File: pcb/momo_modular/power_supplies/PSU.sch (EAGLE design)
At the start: 24 parts, among them IC1 MAX1555

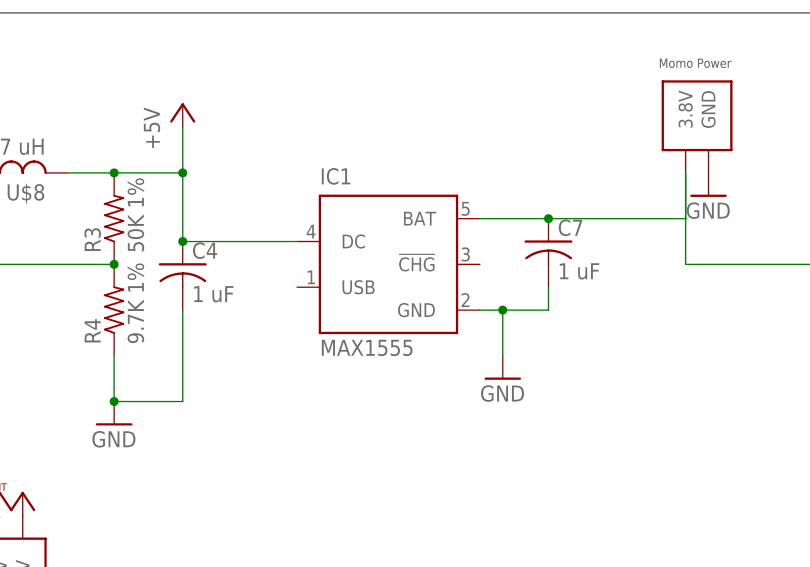
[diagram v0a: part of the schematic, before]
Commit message: Updated schematic and layout to reflect capacitor changes
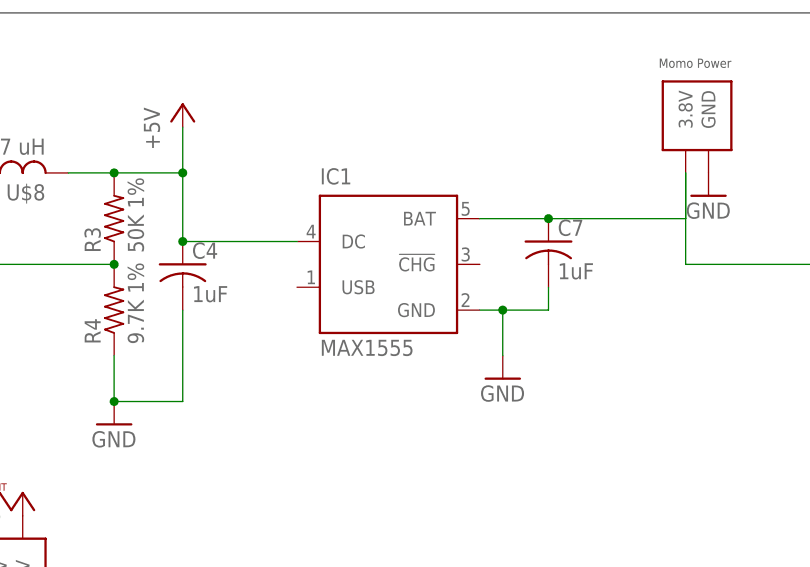
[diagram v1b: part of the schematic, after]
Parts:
- C4, C7: value 1 uF -> 1uF; device rcl:C-USC0805 -> rcl:C-USC0402
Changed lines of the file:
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@@
 <part name="IC1" library="maxim" deviceset="MAX1555" device=""/>
 <part name="GND6" library="supply1" deviceset="GND" device=""/>
-<part name="C4" library="rcl" deviceset="C-US" device="C0805" value="1 uF"/>
-<part name="C7" library="rcl" deviceset="C-US" device="C0805" value="1 uF"/>
 <part name="U$1" library="components" deviceset="MOMO-EDGE-POWER-M" device=""/>
 <part name="U$2" library="components" deviceset="MOMO-EDGE-POWER-M" device=""/>
@@
 <part name="P+5" library="supply1" deviceset="+5V" device=""/>
 <part name="P+6" library="supply1" deviceset="+5V" device=""/>
+<part name="C7" library="rcl" deviceset="C-US" device="C0402" value="1uF"/>
+<part name="C4" library="rcl" deviceset="C-US" device="C0402" value="1uF"/>
 </parts>
 <sheets>
@@
 <instance part="IC1" gate="G$1" x="55.88" y="78.74"/>
 <instance part="GND6" gate="1" x="68.58" y="66.04"/>
-<instance part="C4" gate="G$1" x="33.02" y="78.74"/>
-<instance part="C7" gate="G$1" x="73.66" y="81.28"/>
 <instance part="U$1" gate="G$1" x="-63.5" y="68.58"/>
 <instance part="U$2" gate="G$1" x="91.44" y="91.44" rot="R90"/>
@@
 <instance part="P+5" gate="1" x="48.26" y="27.94"/>
 <instance part="P+6" gate="1" x="30.48" y="2.54"/>
+<instance part="C7" gate="G$1" x="73.66" y="81.28"/>
+<instance part="C4" gate="G$1" x="33.02" y="78.74"/>
 </instances>
 <busses>
@@
 <pinref part="R4" gate="G$1" pin="1"/>
 <pinref part="GND7" gate="1" pin="GND"/>
-<pinref part="C4" gate="G$1" pin="2"/>
 <wire x1="33.02" y1="73.66" x2="33.02" y2="63.5" width="0.1524" layer="91"/>
 <wire x1="33.02" y1="63.5" x2="25.4" y2="63.5" width="0.1524" layer="91"/>
 <wire x1="25.4" y1="63.5" x2="25.4" y2="68.58" width="0.1524" layer="91"/>
 <junction x="25.4" y="63.5"/>
+<pinref part="C4" gate="G$1" pin="2"/>
 </segment>
 <segment>
@@
 <wire x1="68.58" y1="68.58" x2="68.58" y2="73.66" width="0.1524" layer="91"/>
 <wire x1="68.58" y1="73.66" x2="66.04" y2="73.66" width="0.1524" layer="91"/>
-<pinref part="C7" gate="G$1" pin="2"/>
 <wire x1="73.66" y1="76.2" x2="73.66" y2="73.66" width="0.1524" layer="91"/>
 <wire x1="73.66" y1="73.66" x2="68.58" y2="73.66" width="0.1524" layer="91"/>
 <junction x="68.58" y="73.66"/>
+<pinref part="C7" gate="G$1" pin="2"/>
 </segment>
 <segment>
